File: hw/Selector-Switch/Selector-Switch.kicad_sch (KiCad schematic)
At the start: 2 parts, among them U1 FTDI-LC231X

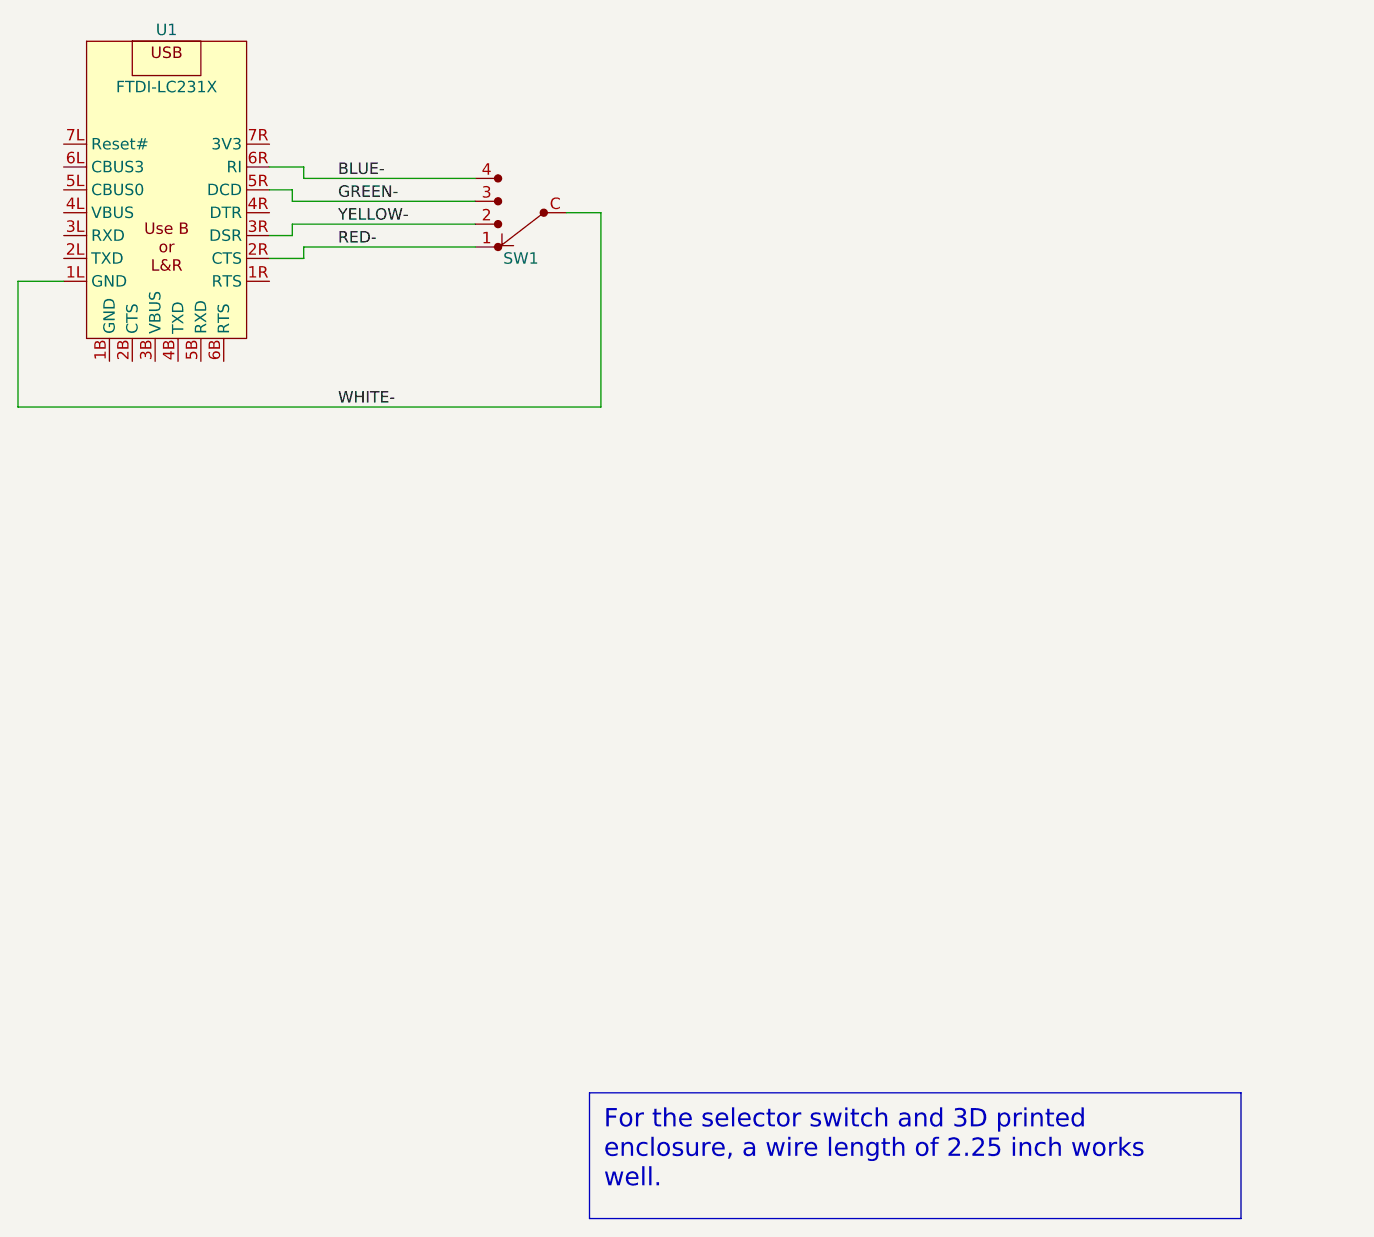
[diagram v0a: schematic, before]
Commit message: SelectorSW: Update schematic
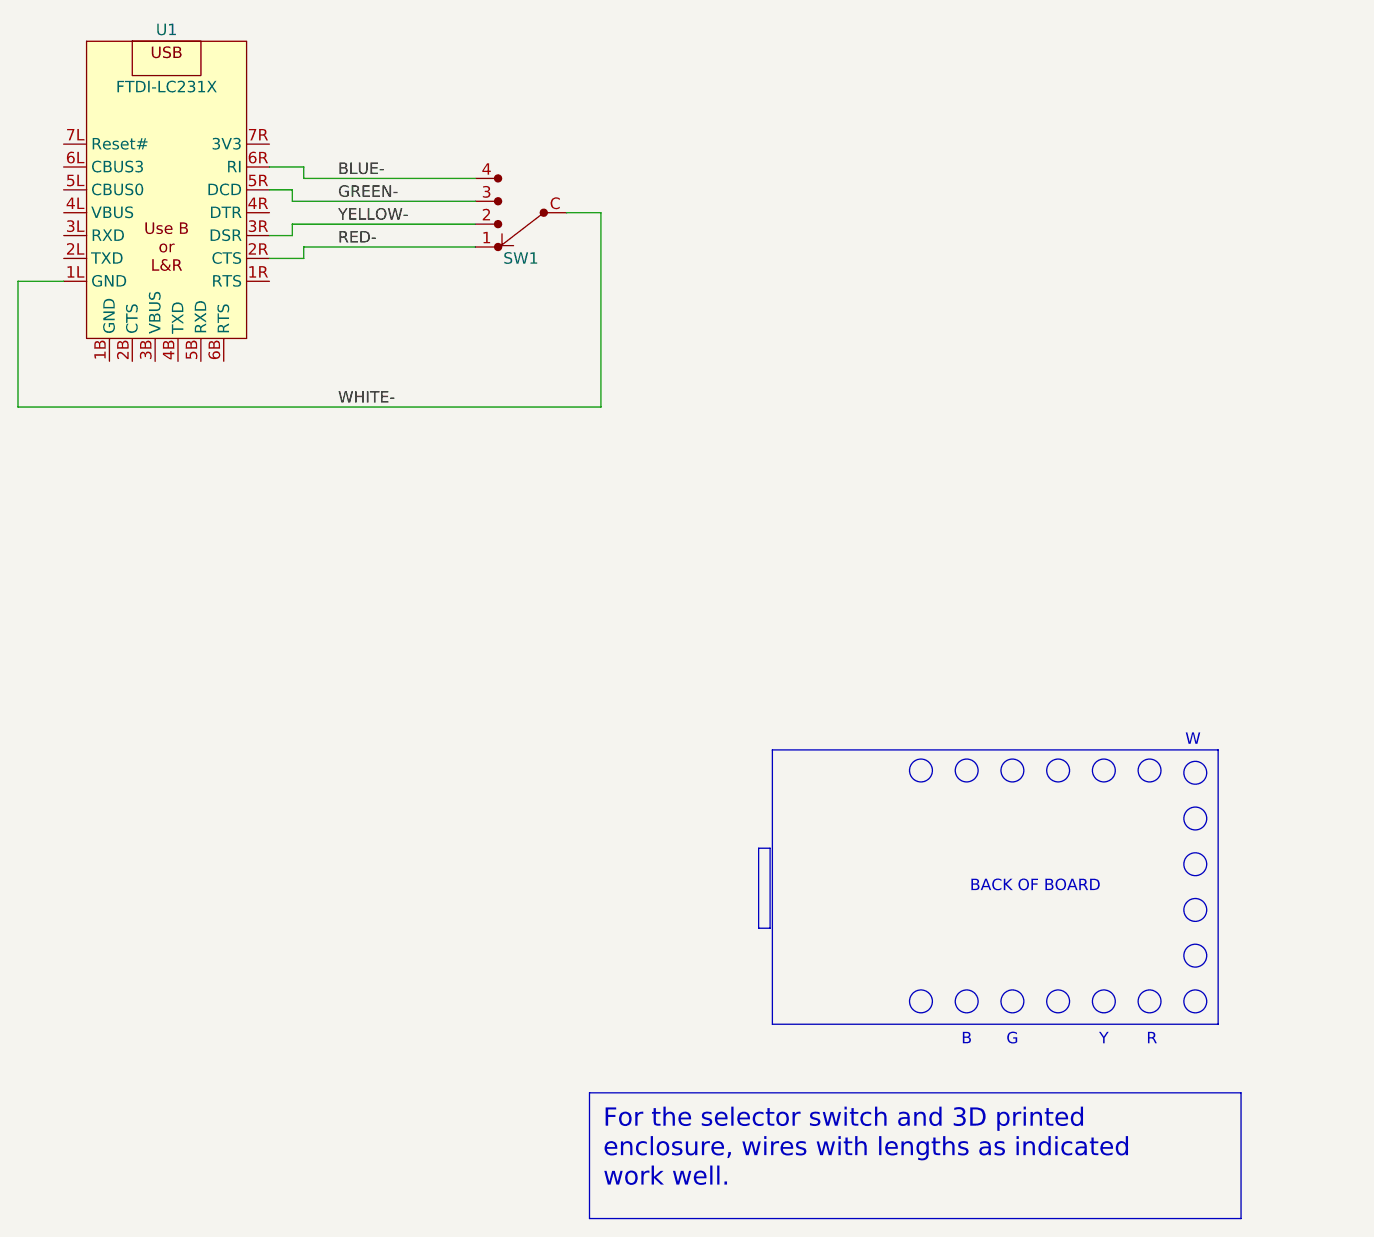
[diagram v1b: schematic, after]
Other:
- note added: "B"
- note added: "BACK OF BOARD"
- note added: "G"
- note added: "R"
- note added: "W"
- note added: "Y"
